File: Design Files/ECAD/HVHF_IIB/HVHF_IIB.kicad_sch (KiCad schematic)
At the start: 79 parts, among them J1 1984963, J2 1984963, J3 731375003, J4 CONSMA002-L, J5 1984963, Q1 PNP, Q2 BFP196E6327HTSA1, T1 BFU590G, T10 BFQ252, T11 BFQ252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

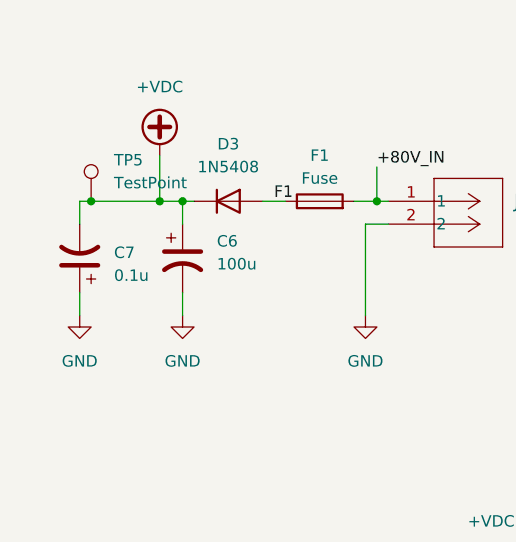
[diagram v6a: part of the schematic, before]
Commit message: checked footprints
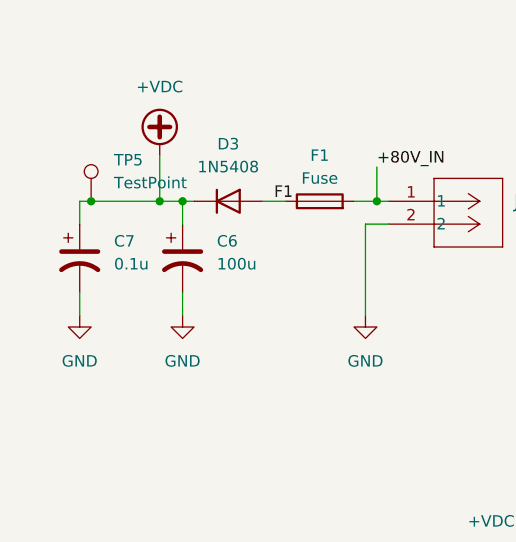
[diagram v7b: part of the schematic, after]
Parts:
- Q1: footprint Package_TO_SOT_SMD:SOT-23-3 -> Library:SOT-23_ONS
- T8: footprint Package_TO_SOT_SMD:SOT-23 -> Library:SOT23_NXP
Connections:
- net +VDC: now also C7.1; no longer C7.2
- net GND: now also C7.2; no longer C7.1
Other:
- moved on the sheet: C7
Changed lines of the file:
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@@
     )
   )
-  (symbol (lib_id "Device:C_Polarized_US") (at 17.78 44.45 180) (unit 1)
-    (in_bom yes) (on_board yes) (dnp no) (fields_autoplaced)
-    (property "Reference" "C7" (at 21.59 43.815 0)
-      (effects (font (size 1.27 1.27)) (justify right))
-    )
-    (property "Value" "0.1u" (at 21.59 46.355 0)
-      (effects (font (size 1.27 1.27)) (justify right))
+  (symbol (lib_id "Device:C_Polarized_US") (at 17.78 44.45 0) (unit 1)
+    (in_bom yes) (on_board yes) (dnp no) (fields_autoplaced)
+    (property "Reference" "C7" (at 21.59 42.545 0)
+      (effects (font (size 1.27 1.27)) (justify left))
+    )
+    (property "Value" "0.1u" (at 21.59 45.085 0)
+      (effects (font (size 1.27 1.27)) (justify left))
     )
     (property "Footprint" "Capacitor_SMD:C_1206_3216Metric_Pad1.33x1.80mm_HandSolder" (at 17.78 44.45 0)
@@
       (effects (font (size 1.27 1.27)) (justify left))
     )
-    (property "Footprint" "Package_TO_SOT_SMD:SOT-23-3" (at 76.2 162.56 0)
+    (property "Footprint" "Library:SOT-23_ONS" (at 76.2 162.56 0)
       (effects (font (size 1.27 1.27)) hide)
     )
@@
       (effects (font (size 1.27 1.27)))
     )
-    (property "Footprint" "Package_TO_SOT_SMD:SOT-23" (at 139.7 172.72 0)
-      (effects (font (size 1.27 1.27)) hide)
-    )
+    (property "Footprint" "Library:SOT23_NXP" (at 139.7 172.72 0)
+      (effects (font (size 1.27 1.27)) hide)
+    )

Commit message: JLC SUBMIT 6/17/2024
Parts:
- C11, C3: value 100n -> 0.1u
- D1: footprint Diode_SMD:D_SOD-123 -> Library:SOD123_MCC-M
- J1, J2, J5: footprint CONN_1984963 -> Library:CONN_1984963
- R10, R9: footprint Resistor_SMD:R_2512_6332Metric -> Library:RC2512N_VIS-M
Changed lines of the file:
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@@
       (effects (font (size 1.524 1.524)) (justify left))
     )
-    (property "Footprint" "CONN_1984963" (at 118.11 58.42 0)
+    (property "Footprint" "Library:CONN_1984963" (at 118.11 58.42 0)
       (effects (font (size 1.27 1.27) italic) hide)
     )
@@
       (effects (font (size 1.27 1.27)) (justify left))
     )
-    (property "Value" "100n" (at 128.27 163.83 0)
+    (property "Value" "0.1u" (at 128.27 163.83 0)
       (effects (font (size 1.27 1.27)) (justify left))
     )
@@
       (effects (font (size 1.524 1.524)) (justify left))
     )
-    (property "Footprint" "CONN_1984963" (at 52.07 38.1 0)
+    (property "Footprint" "Library:CONN_1984963" (at 52.07 38.1 0)
       (effects (font (size 1.27 1.27) italic) hide)
     )
@@
       (effects (font (size 1.524 1.524)) (justify left))
     )
-    (property "Footprint" "CONN_1984963" (at 102.87 38.1 0)
+    (property "Footprint" "Library:CONN_1984963" (at 102.87 38.1 0)
       (effects (font (size 1.27 1.27) italic) hide)
     )
@@
       (effects (font (size 1.27 1.27)))
     )
-    (property "Footprint" "Resistor_SMD:R_2512_6332Metric" (at 86.36 112.522 90)
+    (property "Footprint" "Library:RC2512N_VIS-M" (at 86.36 112.522 90)
       (effects (font (size 1.27 1.27)) hide)
     )
@@
       (effects (font (size 1.27 1.27)))
     )
-    (property "Footprint" "Resistor_SMD:R_2512_6332Metric" (at 97.79 112.522 90)
+    (property "Footprint" "Library:RC2512N_VIS-M" (at 97.79 112.522 90)
       (effects (font (size 1.27 1.27)) hide)
     )
@@
       (effects (font (size 1.27 1.27)))
     )
-    (property "Footprint" "Diode_SMD:D_SOD-123" (at 26.67 167.005 0)
-      (effects (font (size 1.27 1.27)) hide)
-    )
-    (property "Datasheet" "https://www.vishay.com/docs/85748/1n4148w.pdf" (at 26.67 162.56 0)
+    (property "Footprint" "Library:SOD123_MCC-M" (at 26.67 167.005 0)
+      (effects (font (size 1.27 1.27)) hide)
+    )
+    (property "Datasheet" "" (at 26.67 162.56 0)
       (effects (font (size 1.27 1.27)) hide)
     )
@@
       (effects (font (size 1.27 1.27)) (justify left))
     )
-    (property "Value" "100n" (at 118.11 163.83 0)
-      (effects (font (size 1.27 1.27)) (justify left))
-    )
+    (property "Value" "0.1u" (at 118.11 163.83 0)
+      (effects (font (size 1.27 1.27)) (justify left))
+    )
